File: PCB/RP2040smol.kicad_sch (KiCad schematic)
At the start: 41 parts, among them SW1 BOOTSEL, SW2 RESET, U1 MIC5528, U2 RP2040, U3 W25Q64JVZP, Y1 Crystal_520-120-18-33JGN-TR3

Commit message: RevD.
* All small passives are now 0603+
* Pads for RP2040 and MIC5528 have been extended to try to make soldering more reasonable
* Removed WS2812b capacitor. Hopefully the board has enough capacitance without it.
* Rearranged BOOTSEL and Reset buttons
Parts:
- removed C14: 100nF, Capacitor_SMD:C_0402_1005Metric, symbol Device:C_Small
- C10, C11, C13, C15, C16, C17, C4, C5, C6, C9: footprint Capacitor_SMD:C_0402_1005Metric -> Capacitor_SMD:C_0603_1608Metric
- R2: value 33 -> 330
- R3, R4: value 22 -> 27
- R7, R8: footprint Resistor_SMD:R_0402_1005Metric -> Resistor_SMD:R_0603_1608Metric

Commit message: HTML BoM fix - no physical board changes. * Set solder jumpers and castellated pads on schematic to "Exclude from BOM" * Generated RevD BoM HTML
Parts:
- JP1, JP2, JP3, PADS1: now left out of the parts list
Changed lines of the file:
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@@
   )
   (symbol (lib_id "Jumper:Jumper_2_Bridged") (at 233.68 123.19 0) (unit 1)
-    (in_bom yes) (on_board yes) (fields_autoplaced)
+    (in_bom no) (on_board yes) (fields_autoplaced)
     (property "Reference" "JP3" (id 0) (at 233.68 118.5885 0))
     (property "Value" "LED Disable" (id 1) (at 233.68 121.3636 0))
@@
   )
   (symbol (lib_id "Jumper:Jumper_2_Bridged") (at 233.68 109.22 0) (unit 1)
-    (in_bom yes) (on_board yes) (fields_autoplaced)
+    (in_bom no) (on_board yes) (fields_autoplaced)
     (property "Reference" "JP2" (id 0) (at 233.68 104.6185 0))
     (property "Value" "Neopix Disable" (id 1) (at 233.68 107.3936 0))
@@
   )
   (symbol (lib_id "Jumper:Jumper_2_Bridged") (at 233.68 96.52 0) (unit 1)
-    (in_bom yes) (on_board yes) (fields_autoplaced)
+    (in_bom no) (on_board yes) (fields_autoplaced)
     (property "Reference" "JP1" (id 0) (at 233.68 91.9185 0))
     (property "Value" "Neopix Power Disable" (id 1) (at 233.68 94.6936 0))
@@
   )
   (symbol (lib_id "MikeLib:rp2040smol-b-pads") (at 250.19 55.88 0) (unit 1)
-    (in_bom yes) (on_board yes)
+    (in_bom no) (on_board yes)
     (property "Reference" "PADS1" (id 0) (at 264.16 71.12 0)
       (effects (font (size 1.27 1.27)) (justify left))

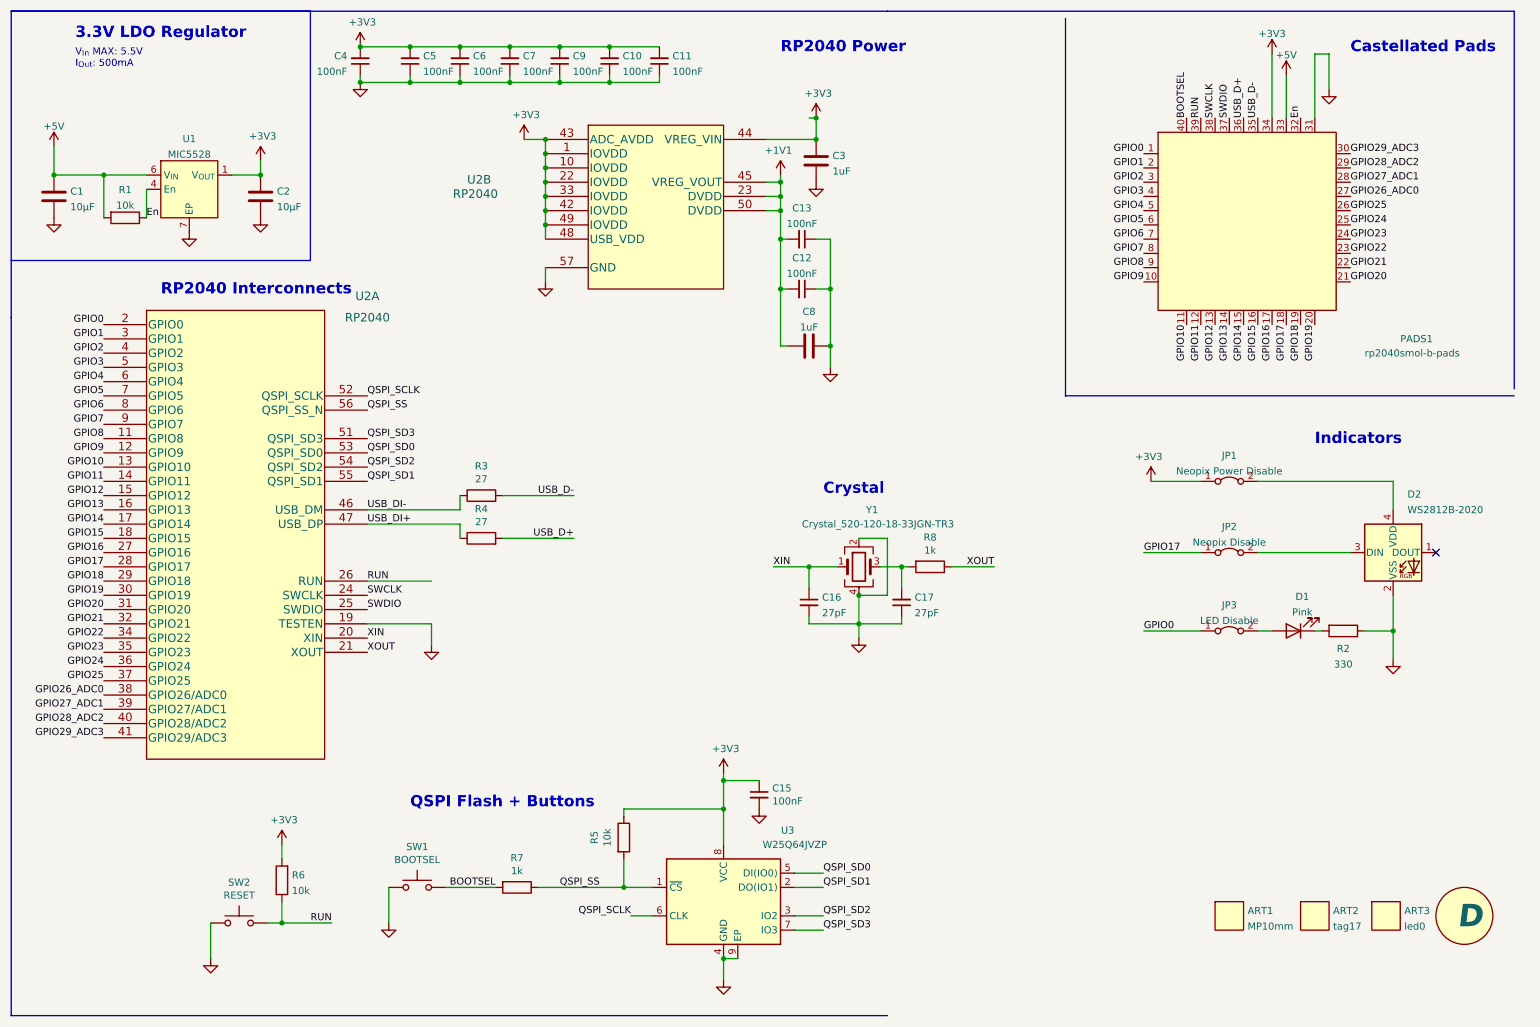
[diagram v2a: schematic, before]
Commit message: * Major schematic tidy * Changed LDO to SOT23-5 AP2112K-3.3
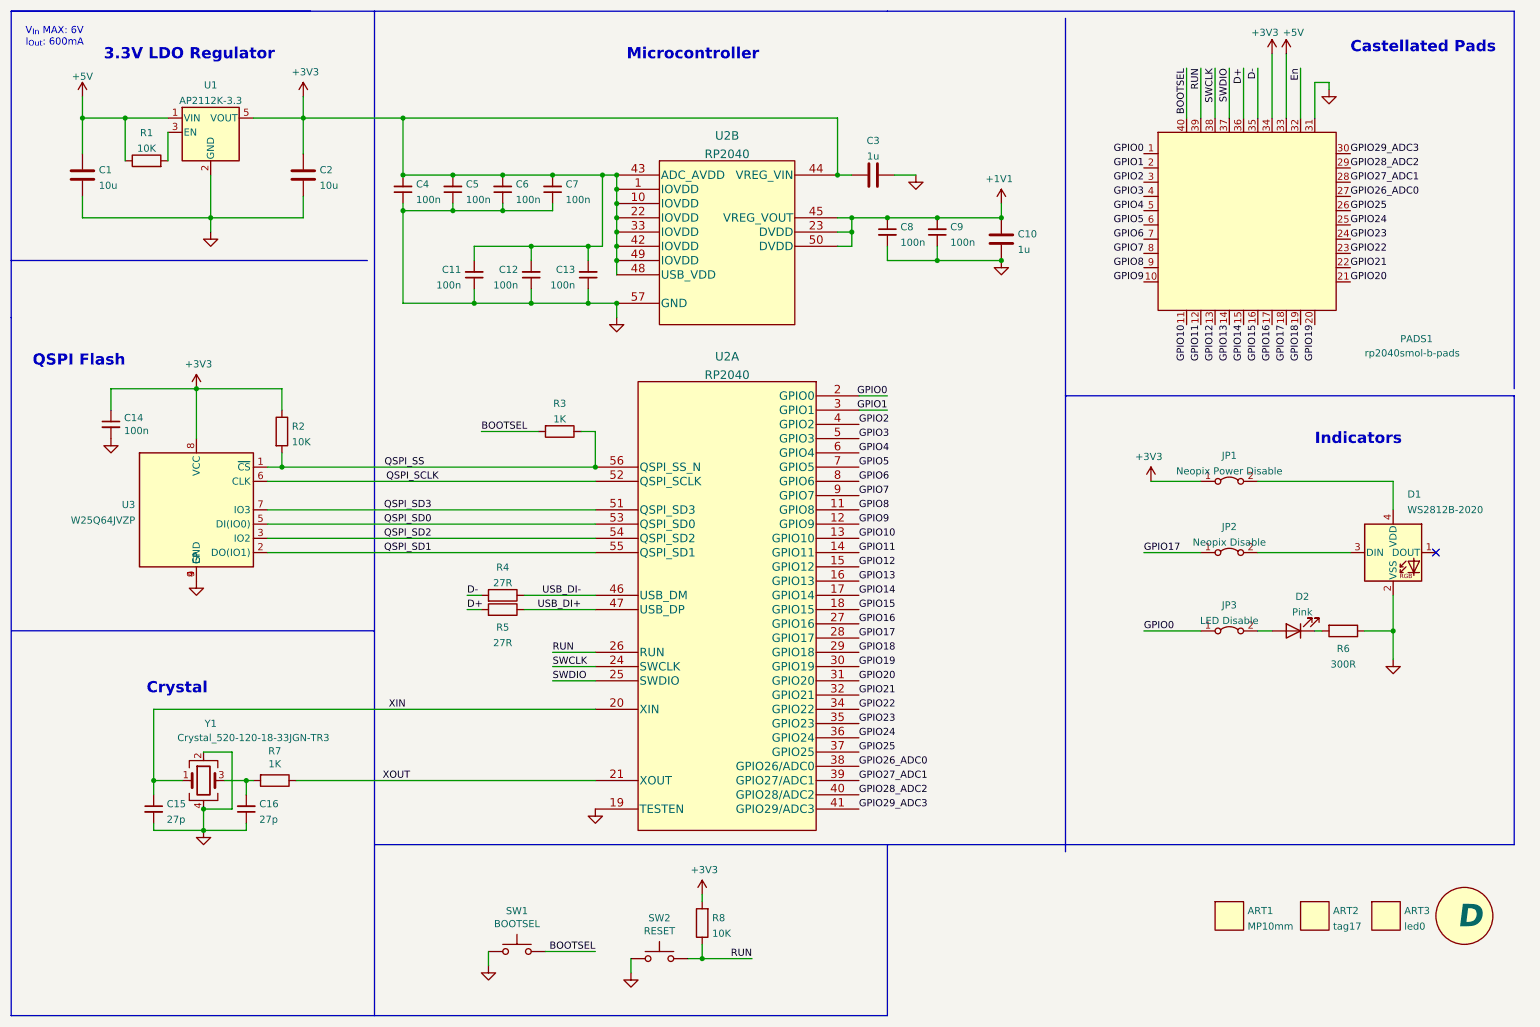
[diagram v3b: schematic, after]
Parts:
- removed U1: MIC5528, MikeFootprintLib:MIC5528_DFN-6-1EP_1.2x1.2mm_P0.4mm_EP0.3x0.94mm_PullBack, symbol MikeLib:MIC5528
- added U1: AP2112K-3.3, Package_TO_SOT_SMD:SOT-23-5, symbol Regulator_Linear:AP2112K-3.3
- C1, C2: value 10µF -> 10u
- C10: renamed from C8; value 1uF -> 1u
- C11: renamed from C6; value 100nF -> 100n
- C12: renamed from C11; value 100nF -> 100n
- C13: renamed from C4; value 100nF -> 100n
- C14: renamed from C15; value 100nF -> 100n
- C15: renamed from C16; value 27pF -> 27p
- C16: renamed from C17; value 27pF -> 27p
- C3: value 1uF -> 1u
- C4: renamed from C10; value 100nF -> 100n
- C5: renamed from C7; value 100nF -> 100n
- C6: renamed from C5; value 100nF -> 100n
- C7: renamed from C9; value 100nF -> 100n
- C8: renamed from C13; value 100nF -> 100n
- C9: renamed from C12; value 100nF -> 100n
- R1: value 10k -> 10K
- R2: renamed from R5; value 10k -> 10K
- R3: renamed from R7; value 1k -> 1K
- R4: renamed from R3; value 27 -> 27R
- R5: renamed from R4; value 27 -> 27R
- R6: renamed from R2; value 330 -> 300R
- R7: renamed from R8; value 1k -> 1K
- R8: renamed from R6; value 10k -> 10K
- U3: symbol MikeLib:W25Q64JVZP -> MikeLib:W25Q64JVZP_Rearranged
- renumbered D2 to D1, D1 to D2
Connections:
- net +1V1: now also C8.1; no longer C8.2
- net +3V3: now also U1.5 (VOUT)
- net +5V: now also R1.1, U1.1 (VIN); no longer R1.2
- net En: no longer R1.1
- net GND: now also C8.2, U1.2 (GND); no longer C8.1
- net USB_D+ renamed D+
- net USB_D- renamed D-
- new net: R1.2, U1.3 (EN)
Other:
- note added: "Microcontroller"
- note added: "QSPI Flash"
- note added: "V_{In} MAX: 6V I_{Out}: 600mA"
- note removed: "QSPI Flash + Buttons"
- note removed: "RP2040 Interconnects"
- note removed: "RP2040 Power"
- note removed: "V_{In} MAX: 5.5V I_{Out}: 500mA"
- moved on the sheet: C1, C10, C11, C12, C13, C14, C15, C16, C2, C3, C4, C5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

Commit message: E
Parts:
- MISC1: value D -> E
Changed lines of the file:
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@@
       (effects (font (size 1.27 1.27)) hide)
     )
-    (property "Value" "D" (id 1) (at 274.32 173.99 0)
+    (property "Value" "E" (id 1) (at 274.32 173.99 0)
       (effects (font (size 4 4) bold italic) (justify left))
     )
@@
     )
     (path "/391dcbac-64b5-4436-a171-22510e2cc165"
-      (reference "MISC1") (unit 1) (value "D") (footprint "MikeFootprintLib:RevisionSymbol_Small")
+      (reference "MISC1") (unit 1) (value "E") (footprint "MikeFootprintLib:RevisionSymbol_Small")
     )
     (path "/6eeba014-e27c-49cf-b969-597642a973b0"

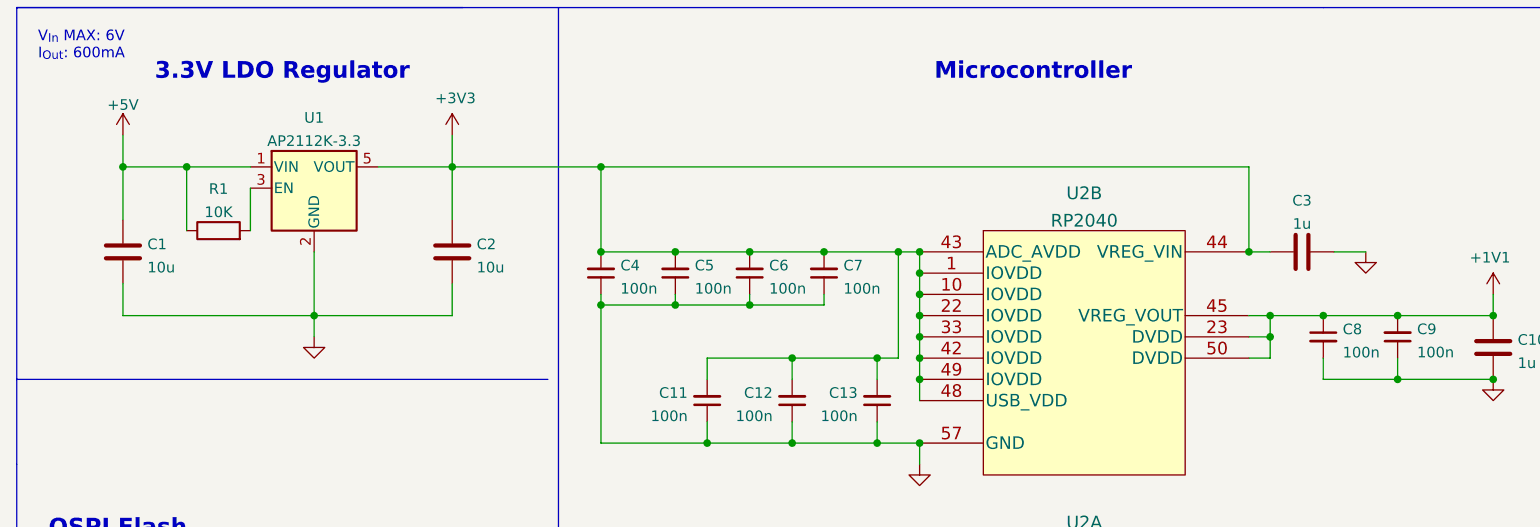
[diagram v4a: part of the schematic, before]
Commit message: Squeezed the bigger LDO onto the board...
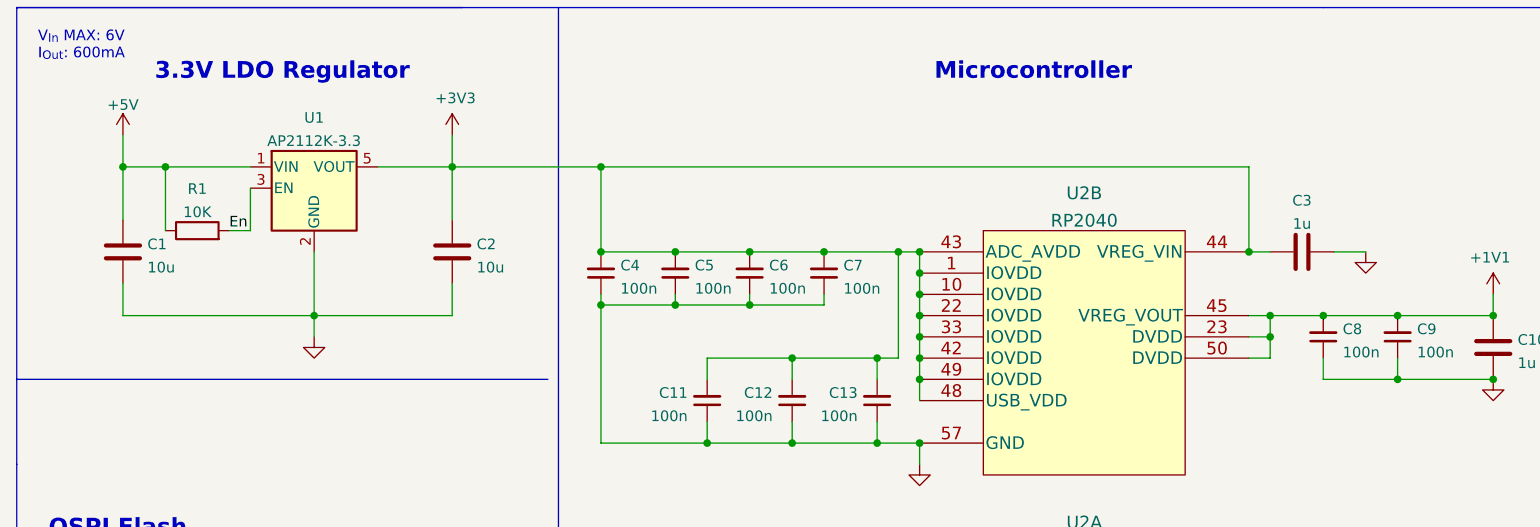
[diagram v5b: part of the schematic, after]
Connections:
- net +1V1: now also C8.2; no longer C8.1
- net En: now also R1.2, U1.3 (EN)
- net GND: now also C8.1; no longer C8.2
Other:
- moved on the sheet: C8, R1
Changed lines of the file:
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@@
   (junction (at 181.61 57.15) (diameter 0) (color 0 0 0 0)
   )
+  (junction (at 34.29 31.75) (diameter 0) (color 0 0 0 0)
+  )
   (junction (at 166.37 49.53) (diameter 0) (color 0 0 0 0)
-  )
-  (junction (at 36.83 31.75) (diameter 0) (color 0 0 0 0)
   )
   (junction (at 124.46 54.61) (diameter 0) (color 0 0 0 0)
@@
     (stroke (width 0) (type default) (color 0 0 0 0))
   )
+  (wire (pts (xy 44.45 39.37) (xy 41.91 39.37))
+    (stroke (width 0) (type default) (color 0 0 0 0))
+  )
   (wire (pts (xy 246.38 22.86) (xy 246.38 31.75))
     (stroke (width 0) (type default) (color 0 0 0 0))
@@
     (stroke (width 0) (type default) (color 0 0 0 0))
   )
-  (wire (pts (xy 29.21 31.75) (xy 36.83 31.75))
+  (wire (pts (xy 29.21 31.75) (xy 34.29 31.75))
     (stroke (width 0) (type default) (color 0 0 0 0))
   )
@@
     (stroke (width 0) (type default) (color 0 0 0 0))
   )
-  (wire (pts (xy 36.83 31.75) (xy 36.83 39.37))
+  (wire (pts (xy 34.29 31.75) (xy 34.29 39.37))
     (stroke (width 0) (type default) (color 0 0 0 0))
   )
@@
     (stroke (width 0) (type default) (color 0 0 0 0))
   )
+  (wire (pts (xy 34.29 31.75) (xy 44.45 31.75))
+    (stroke (width 0) (type default) (color 0 0 0 0))
+  )
   (wire (pts (xy 99.06 64.77) (xy 109.22 64.77))
     (stroke (width 0) (type default) (color 0 0 0 0))
@@
   )
   (wire (pts (xy 113.03 132.08) (xy 120.65 132.08))
-    (stroke (width 0) (type default) (color 0 0 0 0))
-  )
-  (wire (pts (xy 36.83 31.75) (xy 44.45 31.75))
     (stroke (width 0) (type default) (color 0 0 0 0))
   )
@@
   (label "USB_DI+" (at 118.11 119.38 180)
     (effects (font (size 1.27 1.27)) (justify right bottom))
+  )
+  (label "En" (at 41.91 39.37 0)
+    (effects (font (size 1.27 1.27)) (justify left bottom))
   )
   (label "GPIO20" (at 255.27 60.96 0)
@@
     (pin "1")
   )
-  (symbol (lib_id "Device:R") (at 40.64 39.37 90) (unit 1)
-    (in_bom yes) (on_board yes) (fields_autoplaced)
-    (property "Reference" "R1" (id 0) (at 40.64 34.3875 90))
-    (property "Value" "10K" (id 1) (at 40.64 37.1626 90))
-    (property "Footprint" "Resistor_SMD:R_0603_1608Metric" (id 2) (at 40.64 41.148 90)
-      (effects (font (size 1.27 1.27)) hide)
-    )
-    (property "Datasheet" "~" (id 3) (at 40.64 39.37 0)
+  (symbol (lib_id "Device:R") (at 38.1 39.37 90) (unit 1)
+    (in_bom yes) (on_board yes) (fields_autoplaced)
+    (property "Reference" "R1" (id 0) (at 38.1 34.3875 90))
+    (property "Value" "10K" (id 1) (at 38.1 37.1626 90))
+    (property "Footprint" "Resistor_SMD:R_0603_1608Metric" (id 2) (at 38.1 41.148 90)
+      (effects (font (size 1.27 1.27)) hide)
+    )
+    (property "Datasheet" "~" (id 3) (at 38.1 39.37 0)
       (effects (font (size 1.27 1.27)) hide)
     )
@@
     (pin "4")
   )
-  (symbol (lib_id "Device:C_Small") (at 172.72 52.07 0) (unit 1)
-    (in_bom yes) (on_board yes) (fields_autoplaced)
-    (property "Reference" "C8" (id 0) (at 175.0441 51.1678 0)
-      (effects (font (size 1.27 1.27)) (justify left))
-    )
-    (property "Value" "100n" (id 1) (at 175.0441 53.9429 0)
-      (effects (font (size 1.27 1.27)) (justify left))
+  (symbol (lib_id "Device:C_Small") (at 172.72 52.07 180) (unit 1)
+    (in_bom yes) (on_board yes) (fields_autoplaced)
+    (property "Reference" "C8" (id 0) (at 175.0441 51.1551 0)
+      (effects (font (size 1.27 1.27)) (justify right))
+    )
+    (property "Value" "100n" (id 1) (at 175.0441 53.9302 0)
+      (effects (font (size 1.27 1.27)) (justify right))
     )
     (property "Footprint" "Capacitor_SMD:C_0603_1608Metric" (id 2) (at 172.72 52.07 0)

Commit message: m
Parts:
- SW1, SW2: footprint Button_Switch_SMD:SW_SPST_PTS810 -> MikeSwitchFootprints:SW_Push_SPST_Alps_SKRK_Clone
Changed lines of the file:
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@@
     (property "Reference" "SW2" (id 0) (at 132.08 174.371 0))
     (property "Value" "RESET" (id 1) (at 132.08 176.6824 0))
-    (property "Footprint" "Button_Switch_SMD:SW_SPST_PTS810" (id 2) (at 132.08 176.53 0)
+    (property "Footprint" "MikeSwitchFootprints:SW_Push_SPST_Alps_SKRK_Clone" (id 2) (at 132.08 176.53 0)
       (effects (font (size 1.27 1.27)) hide)
     )
@@
     (property "Reference" "SW1" (id 0) (at 106.68 173.101 0))
     (property "Value" "BOOTSEL" (id 1) (at 106.68 175.4124 0))
-    (property "Footprint" "Button_Switch_SMD:SW_SPST_PTS810" (id 2) (at 106.68 175.26 0)
+    (property "Footprint" "MikeSwitchFootprints:SW_Push_SPST_Alps_SKRK_Clone" (id 2) (at 106.68 175.26 0)
       (effects (font (size 1.27 1.27)) hide)
     )
@@
     )
     (path "/7e536656-9180-4bdb-b0bb-00f3e70f1632"
-      (reference "SW1") (unit 1) (value "BOOTSEL") (footprint "Button_Switch_SMD:SW_SPST_PTS810")
+      (reference "SW1") (unit 1) (value "BOOTSEL") (footprint "MikeSwitchFootprints:SW_Push_SPST_Alps_SKRK_Clone")
     )
     (path "/21831e86-7f77-448d-b255-ff94c0e692fa"
-      (reference "SW2") (unit 1) (value "RESET") (footprint "Button_Switch_SMD:SW_SPST_PTS810")
+      (reference "SW2") (unit 1) (value "RESET") (footprint "MikeSwitchFootprints:SW_Push_SPST_Alps_SKRK_Clone")
     )
     (path "/72059e0e-070a-4a12-8db0-d7d308cd846a"
